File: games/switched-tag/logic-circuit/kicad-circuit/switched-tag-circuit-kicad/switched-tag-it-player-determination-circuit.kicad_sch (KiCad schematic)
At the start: 16 parts

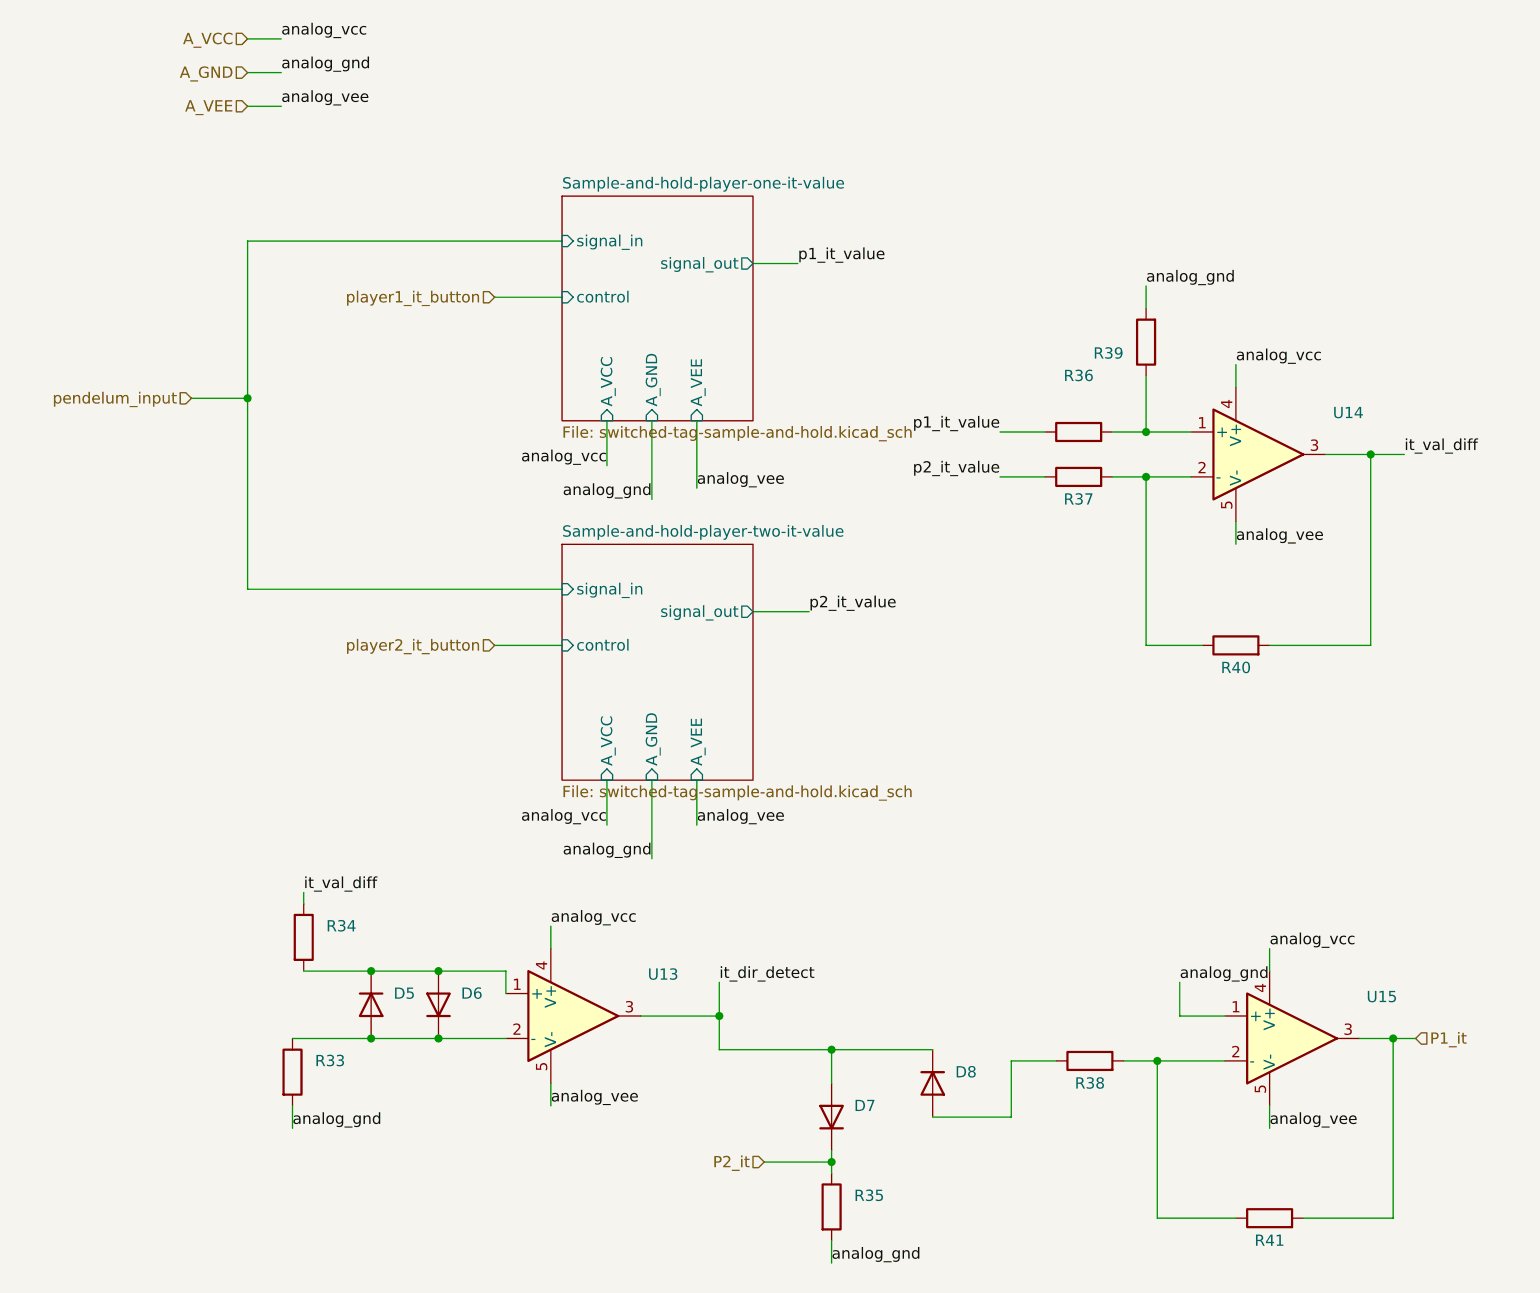
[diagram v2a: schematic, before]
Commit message: Changed spice model of opamp in kicad sim. Fixed design error in it player determination in ltspice and kicad schematic
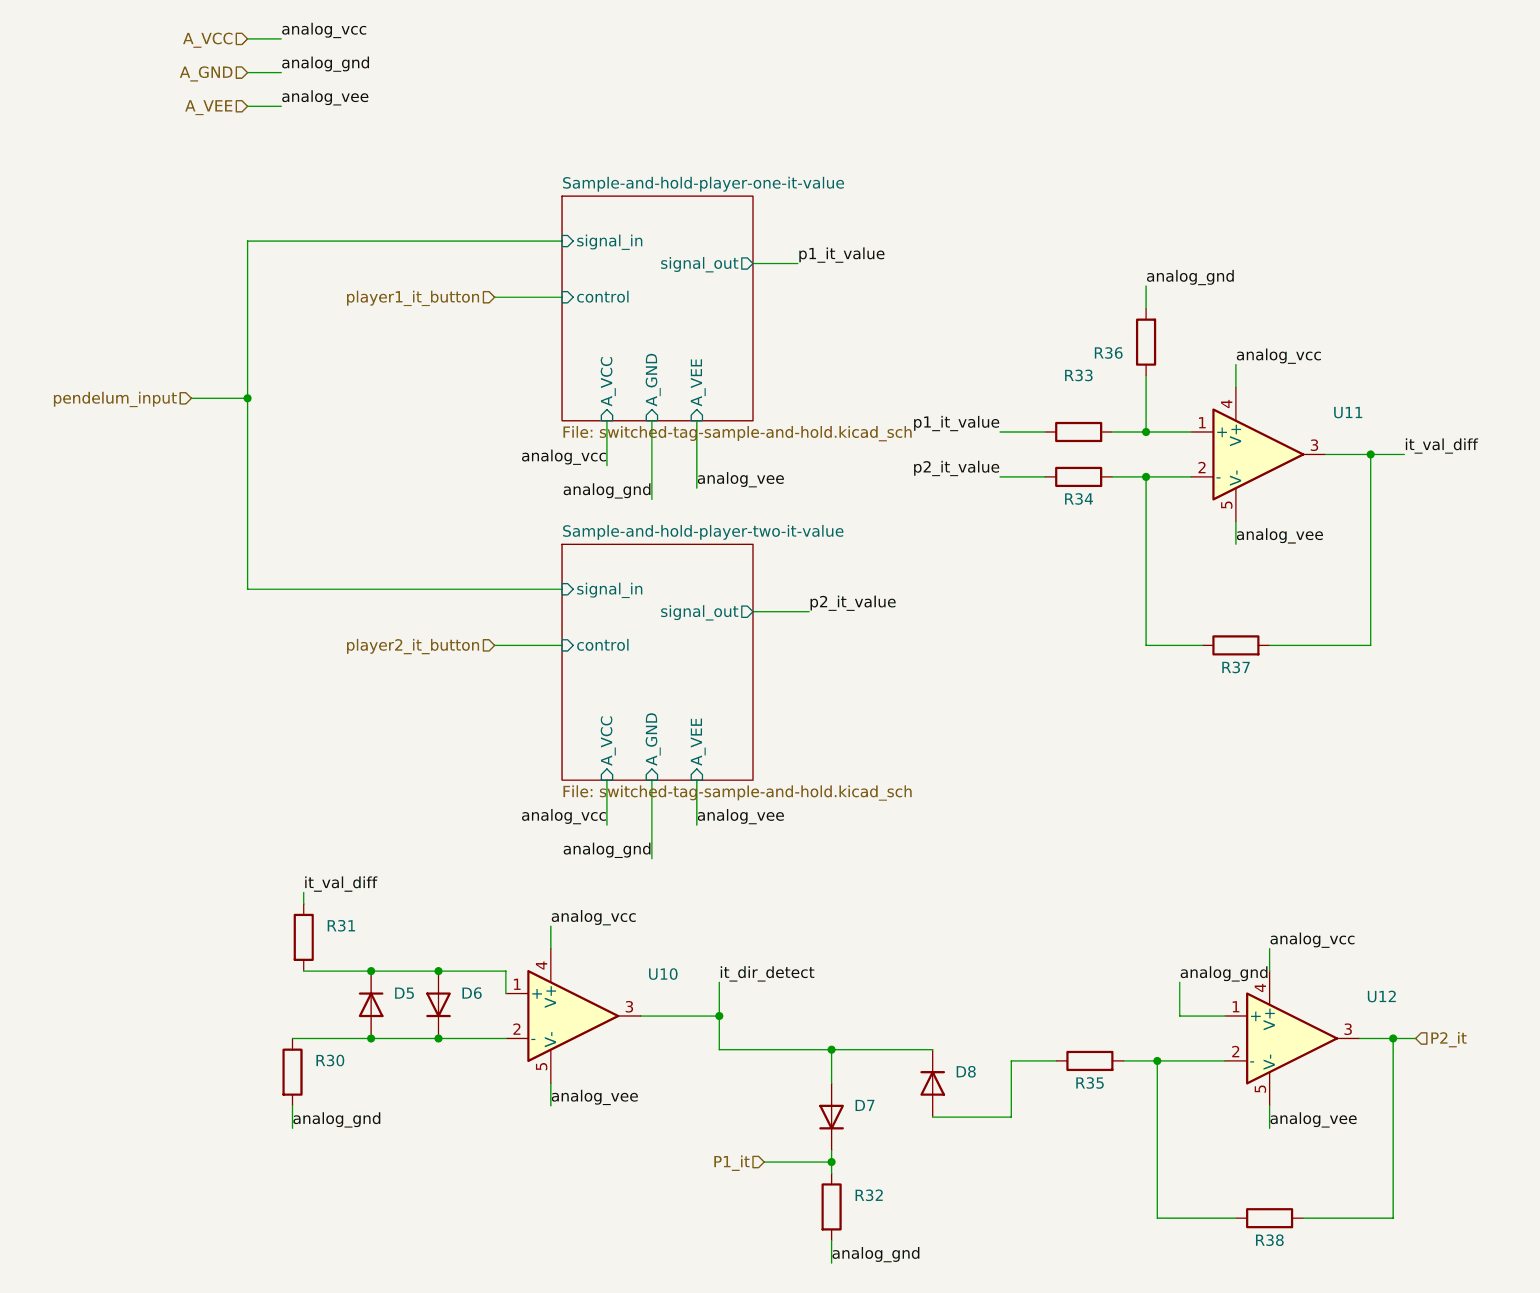
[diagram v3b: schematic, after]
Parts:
- U10: renamed from U13; Spice_Lib_File /home/pab/Inventions/analog-circuit-game-console/ms-circuit-video-games/spice-models/LM358-onsemi.mod -> /home/pab/Inventions/analog-circuit-game-console/ms-circuit-video-games/spice-models/ada4692.mod; Spice_Model LM358 -> ADA4692
- U11: renamed from U14; Spice_Lib_File /home/pab/Inventions/analog-circuit-game-console/ms-circuit-video-games/spice-models/LM358-onsemi.mod -> /home/pab/Inventions/analog-circuit-game-console/ms-circuit-video-games/spice-models/ada4692.mod; Spice_Model LM358 -> ADA4692
- U12: renamed from U15; Spice_Lib_File /home/pab/Inventions/analog-circuit-game-console/ms-circuit-video-games/spice-models/LM358-onsemi.mod -> /home/pab/Inventions/analog-circuit-game-console/ms-circuit-video-games/spice-models/ada4692.mod; Spice_Model LM358 -> ADA4692
- renumbered R33 to R30, R34 to R31, R35 to R32, R36 to R33, R37 to R34, R38 to R35, R39 to R36, R40 to R37, R41 to R38
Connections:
- net P1_it: now also D7.1 (K), R32.1; no longer R38.2, U12.3
- net P2_it: now also R38.2, U12.3; no longer D7.1 (K), R32.1
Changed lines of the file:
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@@
     (effects (font (size 1.27 1.27)) (justify left bottom))
   )
-  (hierarchical_label "P2_it" (shape input) (at 96.52 161.29 180)
-    (effects (font (size 1.27 1.27)) (justify right))
+  (hierarchical_label "P2_it" (shape input) (at 170.18 147.32 0)
+    (effects (font (size 1.27 1.27)) (justify left))
   )
   (hierarchical_label "pendelum_input" (shape input) (at 31.75 74.93 180)
@@
     (effects (font (size 1.27 1.27)) (justify right))
   )
-  (hierarchical_label "P1_it" (shape input) (at 170.18 147.32 0)
-    (effects (font (size 1.27 1.27)) (justify left))
+  (hierarchical_label "P1_it" (shape input) (at 96.52 161.29 180)
+    (effects (font (size 1.27 1.27)) (justify right))
   )
   (hierarchical_label "A_VCC" (shape input) (at 38.1 34.29 180)
@@
   (symbol (lib_id "Simulation_SPICE:OPAMP") (at 74.93 144.78 0) (unit 1)
     (in_bom yes) (on_board yes) (fields_autoplaced)
-    (property "Reference" "U13" (id 0) (at 85.09 140.081 0))
+    (property "Reference" "U10" (id 0) (at 85.09 140.081 0))
     (property "Value" "" (id 1) (at 85.09 142.621 0))
     (property "Footprint" "" (id 2) (at 74.93 144.78 0)
@@
       (effects (font (size 1.27 1.27)) (justify left) hide)
     )
-    (property "Spice_Model" "LM358" (id 6) (at 74.93 144.78 0)
-      (effects (font (size 1.27 1.27)) hide)
-    )
-    (property "Spice_Lib_File" "/home/pab/Inventions/analog-circuit-game-console/ms-circuit-video-games/spice-models/LM358-onsemi.mod" (id 7) (at 74.93 144.78 0)
+    (property "Spice_Model" "ADA4692" (id 6) (at 74.93 144.78 0)
+      (effects (font (size 1.27 1.27)) hide)
+    )
+    (property "Spice_Lib_File" "/home/pab/Inventions/analog-circuit-game-console/ms-circuit-video-games/spice-models/ada4692.mod" (id 7) (at 74.93 144.78 0)
       (effects (font (size 1.27 1.27)) hide)
     )
@@
   (symbol (lib_id "Device:R") (at 132.08 78.74 90) (unit 1)
     (in_bom yes) (on_board yes) (fields_autoplaced)
-    (property "Reference" "R36" (id 0) (at 132.08 72.39 90))
+    (property "Reference" "R33" (id 0) (at 132.08 72.39 90))
     (property "Value" "" (id 1) (at 132.08 74.93 90))
     (property "Footprint" "" (id 2) (at 132.08 80.518 90)
@@
   (symbol (lib_id "Simulation_SPICE:OPAMP") (at 156.21 147.32 0) (unit 1)
     (in_bom yes) (on_board yes) (fields_autoplaced)
-    (property "Reference" "U15" (id 0) (at 166.37 142.621 0))
+    (property "Reference" "U12" (id 0) (at 166.37 142.621 0))
     (property "Value" "" (id 1) (at 166.37 145.161 0))
     (property "Footprint" "" (id 2) (at 156.21 147.32 0)
@@
       (effects (font (size 1.27 1.27)) (justify left) hide)
     )
-    (property "Spice_Model" "LM358" (id 6) (at 156.21 147.32 0)
-      (effects (font (size 1.27 1.27)) hide)
-    )
-    (property "Spice_Lib_File" "/home/pab/Inventions/analog-circuit-game-console/ms-circuit-video-games/spice-models/LM358-onsemi.mod" (id 7) (at 156.21 147.32 0)
+    (property "Spice_Model" "ADA4692" (id 6) (at 156.21 147.32 0)
+      (effects (font (size 1.27 1.27)) hide)
+    )
+    (property "Spice_Lib_File" "/home/pab/Inventions/analog-circuit-game-console/ms-circuit-video-games/spice-models/ada4692.mod" (id 7) (at 156.21 147.32 0)
       (effects (font (size 1.27 1.27)) hide)
     )
@@
   (symbol (lib_id "Device:R") (at 44.45 135.89 0) (unit 1)
     (in_bom yes) (on_board yes) (fields_autoplaced)
-    (property "Reference" "R34" (id 0) (at 46.99 134.6199 0)
+    (property "Reference" "R31" (id 0) (at 46.99 134.6199 0)
       (effects (font (size 1.27 1.27)) (justify left))
     )
@@
   (symbol (lib_id "Device:R") (at 104.14 166.37 0) (unit 1)
     (in_bom yes) (on_board yes) (fields_autoplaced)
-    (property "Reference" "R35" (id 0) (at 106.68 165.0999 0)
+    (property "Reference" "R32" (id 0) (at 106.68 165.0999 0)
       (effects (font (size 1.27 1.27)) (justify left))
     )
@@
   (symbol (lib_id "Simulation_SPICE:OPAMP") (at 152.4 81.28 0) (unit 1)
     (in_bom yes) (on_board yes) (fields_autoplaced)
-    (property "Reference" "U14" (id 0) (at 162.56 76.581 0))
+    (property "Reference" "U11" (id 0) (at 162.56 76.581 0))
     (property "Value" "" (id 1) (at 162.56 79.121 0))
     (property "Footprint" "" (id 2) (at 152.4 81.28 0)
@@
       (effects (font (size 1.27 1.27)) (justify left) hide)
     )
-    (property "Spice_Model" "LM358" (id 6) (at 152.4 81.28 0)
-      (effects (font (size 1.27 1.27)) hide)
-    )
-    (property "Spice_Lib_File" "/home/pab/Inventions/analog-circuit-game-console/ms-circuit-video-games/spice-models/LM358-onsemi.mod" (id 7) (at 152.4 81.28 0)
+    (property "Spice_Model" "ADA4692" (id 6) (at 152.4 81.28 0)
+      (effects (font (size 1.27 1.27)) hide)
+    )
+    (property "Spice_Lib_File" "/home/pab/Inventions/analog-circuit-game-console/ms-circuit-video-games/spice-models/ada4692.mod" (id 7) (at 152.4 81.28 0)
       (effects (font (size 1.27 1.27)) hide)
     )
@@
   (symbol (lib_id "Device:R") (at 43.18 151.13 0) (unit 1)
     (in_bom yes) (on_board yes) (fields_autoplaced)
-    (property "Reference" "R33" (id 0) (at 45.72 149.8599 0)
+    (property "Reference" "R30" (id 0) (at 45.72 149.8599 0)
       (effects (font (size 1.27 1.27)) (justify left))
     )
@@
   (symbol (lib_id "Device:R") (at 149.86 102.87 90) (unit 1)
     (in_bom yes) (on_board yes)
-    (property "Reference" "R40" (id 0) (at 149.86 105.41 90))
+    (property "Reference" "R37" (id 0) (at 149.86 105.41 90))
     (property "Value" "" (id 1) (at 149.86 107.95 90))
     (property "Footprint" "" (id 2) (at 149.86 104.648 90)
@@
   (symbol (lib_id "Device:R") (at 132.08 83.82 90) (unit 1)
     (in_bom yes) (on_board yes)
-    (property "Reference" "R37" (id 0) (at 132.08 86.36 90))
+    (property "Reference" "R34" (id 0) (at 132.08 86.36 90))
     (property "Value" "" (id 1) (at 132.08 88.9 90))
     (property "Footprint" "" (id 2) (at 132.08 85.598 90)
@@
   (symbol (lib_id "Device:R") (at 133.35 149.86 90) (unit 1)
     (in_bom yes) (on_board yes)
-    (property "Reference" "R38" (id 0) (at 133.35 152.4 90))
+    (property "Reference" "R35" (id 0) (at 133.35 152.4 90))
     (property "Value" "" (id 1) (at 133.35 154.94 90))
     (property "Footprint" "" (id 2) (at 133.35 151.638 90)
@@
   (symbol (lib_id "Device:R") (at 153.67 167.64 90) (unit 1)
     (in_bom yes) (on_board yes)
-    (property "Reference" "R41" (id 0) (at 153.67 170.18 90))
+    (property "Reference" "R38" (id 0) (at 153.67 170.18 90))
     (property "Value" "" (id 1) (at 153.67 172.72 90))
     (property "Footprint" "" (id 2) (at 153.67 169.418 90)
@@
   (symbol (lib_id "Device:R") (at 139.7 68.58 180) (unit 1)
     (in_bom yes) (on_board yes) (fields_autoplaced)
-    (property "Reference" "R39" (id 0) (at 137.16 69.8501 0)
-      (effects (font (size 1.27 1.27)) (justify left))
-    )
+    (property "Reference" "R36" (id 0) (at 137.16 69.8501 0)
+      (effects (font (size 1.27 1.27)) (justify left))
+    )
